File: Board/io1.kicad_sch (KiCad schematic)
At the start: 13 parts, among them J11 Conn_01x09, J12 Conn_01x09, P5 CBMTAPE, U1 XC6SLX9-TQG144, U15 ADM560, X3 M09HPS

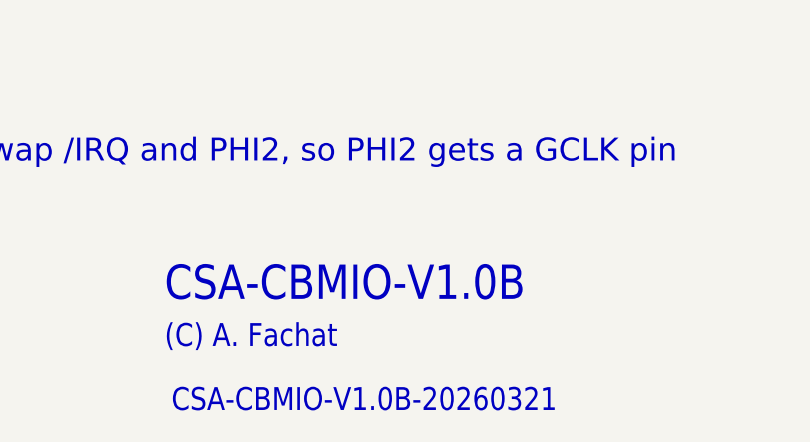
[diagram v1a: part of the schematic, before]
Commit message: add par ATNA, separate kbd cons, kbd serial input to get more I/O
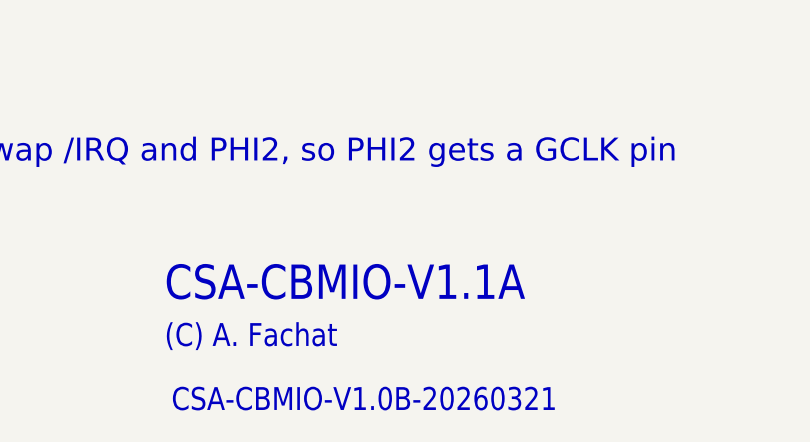
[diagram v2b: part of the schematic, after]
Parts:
- P9: value ~ -> (none)
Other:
- note added: "CSA-CBMIO-V1.1A"
- note removed: "CSA-CBMIO-V1.0B"

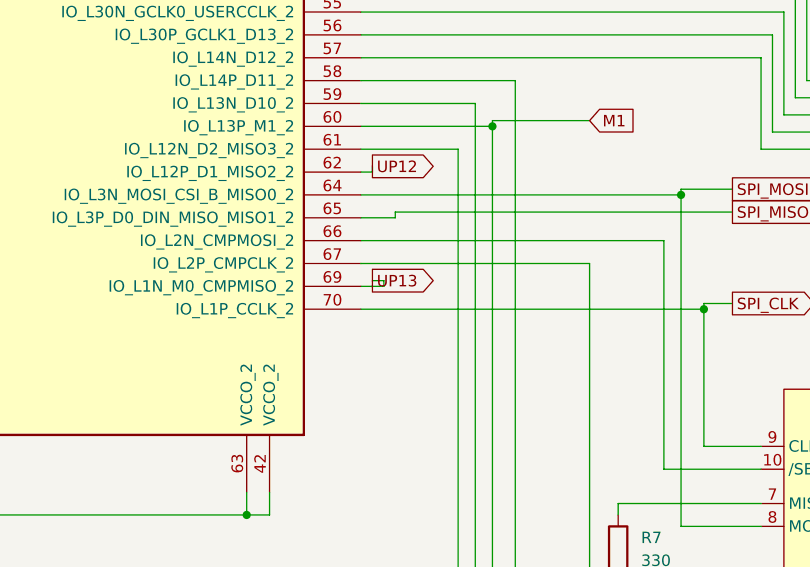
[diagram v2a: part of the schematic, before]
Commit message: schem draft done, layout work started
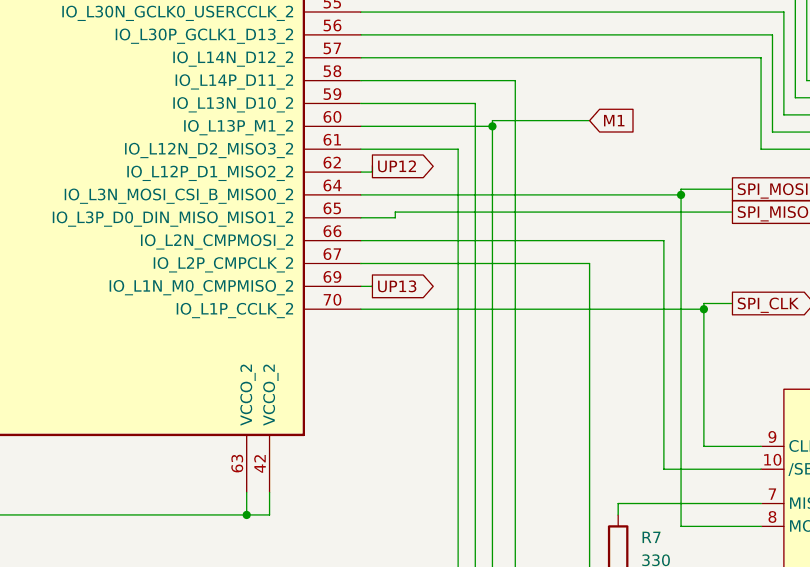
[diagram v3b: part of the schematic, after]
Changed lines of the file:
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@@
 	(wire
 		(pts
-			(xy 193.04 180.34) (xy 195.58 180.34)
+			(xy 193.04 180.34) (xy 194.31 180.34)
 		)
 		(stroke
@@
 	(wire
 		(pts
-			(xy 195.58 180.34) (xy 195.58 179.705)
-		)
-		(stroke
-			(width 0)
-			(type default)
-		)
-	)
-	(wire
-		(pts
 			(xy 86.36 124.46) (xy 91.44 124.46)
 		)
@@
 		(pts
 			(xy 104.14 205.74) (xy 106.68 205.74)
-		)
-		(stroke
-			(width 0)
-			(type default)
-		)
-	)
-	(wire
-		(pts
-			(xy 195.58 179.705) (xy 194.31 179.705)
 		)
 		(stroke
@@
 	(global_label "UP13"
 		(shape output)
-		(at 194.31 179.705 0)
+		(at 194.31 180.34 0)
 		(fields_autoplaced yes)
 		(effects
@@
 		)
 		(property "Intersheetrefs" "${INTERSHEET_REFS}"
-			(at 202.3147 179.705 0)
+			(at 202.3147 180.34 0)
 			(hide yes)
 			(show_name no)
